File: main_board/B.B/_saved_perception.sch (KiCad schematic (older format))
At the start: 10 parts

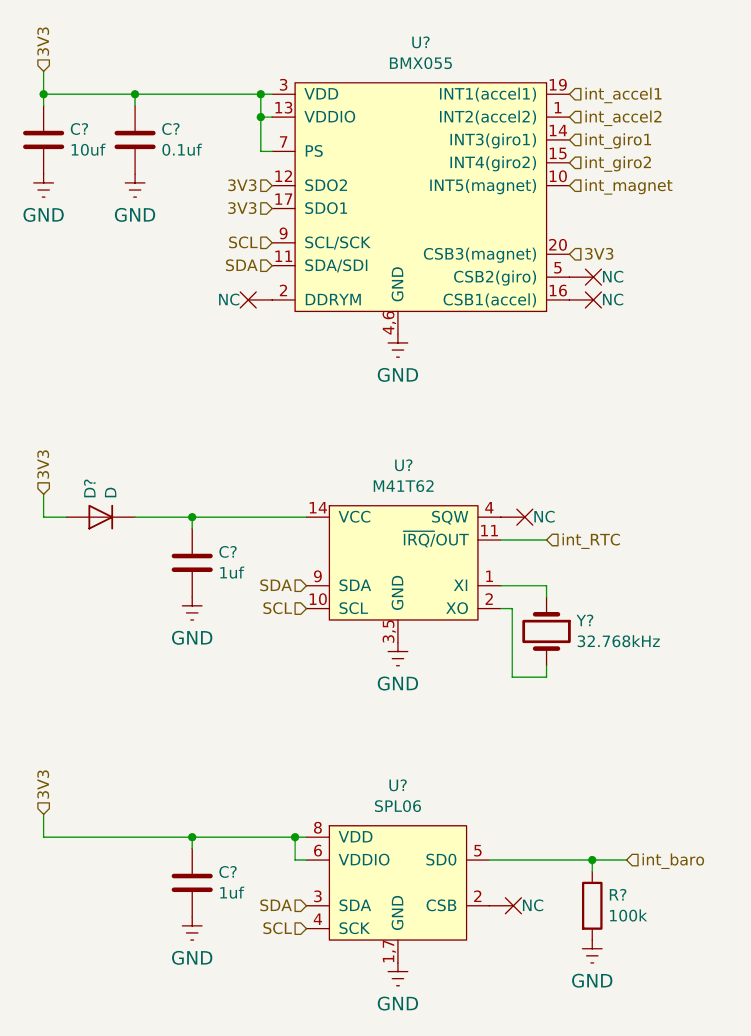
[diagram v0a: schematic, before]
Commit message: interrupt
all interapt on PCA9555
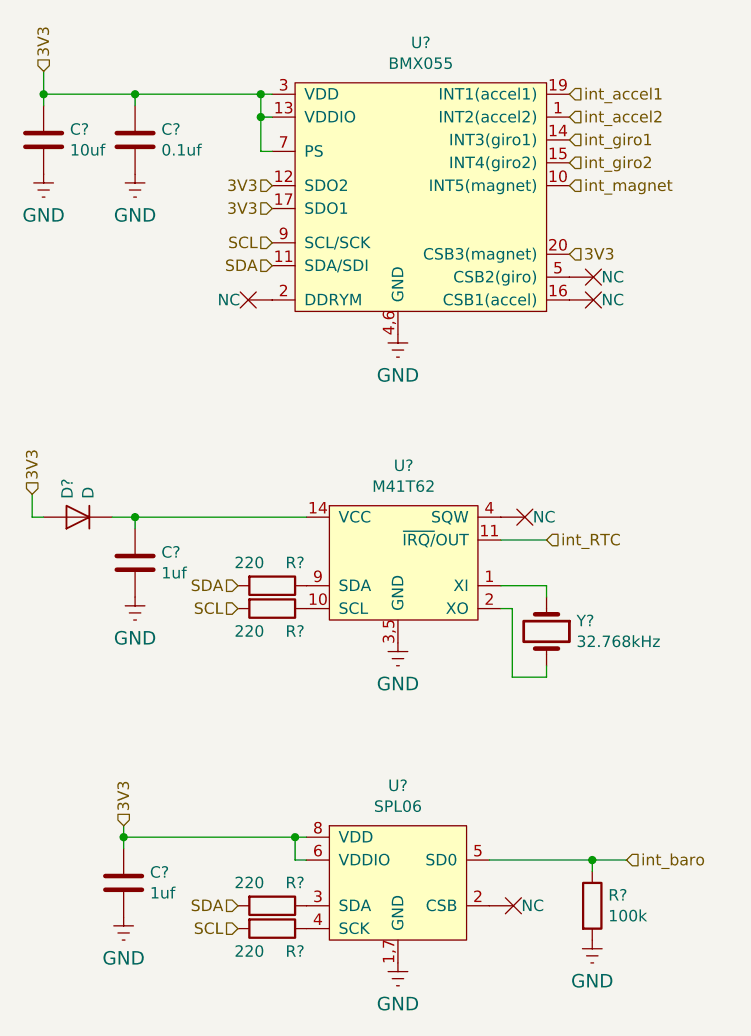
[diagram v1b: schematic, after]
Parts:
- added R? (x4): 220, symbol Device:R
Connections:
- net SCL: now also R?.2, R?.2; no longer U?.10 (SCL), U?.4 (SCK)
- net SDA: now also R?.2, R?.2; no longer U?.3 (SDA), U?.9 (SDA)
- new net: R?.1, U?.10 (SCL)
- new net: R?.1, U?.9 (SDA)
- new net: R?.1, U?.3 (SDA)
- new net: R?.1, U?.4 (SCK)
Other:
- moved on the sheet: C?, D?
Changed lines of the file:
@@
 F 1 "M41T62" H 5625 3884 50  0000 C CNN
 F 2 "" H 5600 3750 50  0001 C CNN
-F 3 "" H 5600 3750 50  0001 C CNN
+F 3 "https://datasheet.lcsc.com/szlcsc/STMicroelectronics-M41T62Q6F_C113207.pdf" H 5600 3750 50  0001 C CNN
 	1    5600 3750
 	1    0    0    -1
 $EndComp
-Text HLabel 4050 3650 1    50   Input ~ 0
+Text HLabel 4000 3650 1    50   Input ~ 0
 3V3
 $Comp
 L Device:D D?
 U 1 1 5F93AF19
-P 4300 3750
+P 4200 3750
 AR Path="/5F96CFDA/5F93AF19" Ref="D?"  Part="1"
 AR Path="/5F9EE529/5F9F24D4/5F93AF19" Ref="D?"  Part="1"
 AR Path="/5FA9DBB3/5F9F24D4/5F93AF19" Ref="D?"  Part="1"
-F 0 "D?" V 4346 3670 50  0000 R CNN
-F 1 "D" V 4255 3670 50  0000 R CNN
-F 2 "BB:SOD-323" H 4300 3750 50  0001 C CNN
-F 3 "https://datasheet.lcsc.com/szlcsc/SK-SD103AWS_C109204.pdf" H 4300 3750 50  0001 C CNN
-F 4 "C109204" V 4300 3750 50  0001 C CNN "LCSC"
-	1    4300 3750
+F 0 "D?" V 4246 3670 50  0000 R CNN
+F 1 "D" V 4155 3670 50  0000 R CNN
+F 2 "BB:SOD-323" H 4200 3750 50  0001 C CNN
+F 3 "https://datasheet.lcsc.com/szlcsc/SK-SD103AWS_C109204.pdf" H 4200 3750 50  0001 C CNN
+F 4 "C109204" V 4200 3750 50  0001 C CNN "LCSC"
+	1    4200 3750
 	-1   0    0    1
 $EndComp
 Wire Wire Line
-	4150 3750 4050 3750
-Wire Wire Line
-	4050 3750 4050 3650
+	4050 3750 4000 3750
+Wire Wire Line
+	4000 3750 4000 3650
 $Comp
 L Device:Crystal Y?
@@
 Wire Wire Line
 	6250 4450 6250 4400
-Text HLabel 5200 4050 0    50   Input ~ 0
-SDA
-Text HLabel 5200 4150 0    50   Input ~ 0
-SCL
 $Comp
 L B.B-eagle-import:GND #GND?
@@
 L B.B-eagle-import:GND #GND?
 U 1 1 5F94A059
-P 4700 4200
+P 4450 4200
 AR Path="/5F96CFDA/5F94A059" Ref="#GND?"  Part="1"
 AR Path="/5F9EE529/5F9F24D4/5F94A059" Ref="#GND?"  Part="1"
 AR Path="/5FA9DBB3/5F9F24D4/5F94A059" Ref="#GND?"  Part="1"
-F 0 "#GND?" H 4700 4200 50  0001 C CNN
-F 1 "GND" H 4700 4120 59  0000 C CNN
-F 2 "" H 4700 4200 50  0001 C CNN
-F 3 "" H 4700 4200 50  0001 C CNN
-	1    4700 4200
-	1    0    0    -1
-$EndComp
-Wire Wire Line
-	4700 3800 4700 3750
+F 0 "#GND?" H 4450 4200 50  0001 C CNN
+F 1 "GND" H 4450 4120 59  0000 C CNN
+F 2 "" H 4450 4200 50  0001 C CNN
+F 3 "" H 4450 4200 50  0001 C CNN
+	1    4450 4200
+	1    0    0    -1
+$EndComp
+Wire Wire Line
+	4450 3800 4450 3750
 $Comp
 L B.B-eagle-import:NC #NC?
@@
 	1    0    0    -1
 $EndComp
-Text HLabel 5200 5550 0    50   Input ~ 0
+Text HLabel 4900 5550 0    50   Input ~ 0
 SCL
-Text HLabel 5200 5450 0    50   Input ~ 0
+Text HLabel 4900 5450 0    50   Input ~ 0
 SDA
 Connection ~ 6450 5250
@@
 	-1   0    0    1
 $EndComp
-Text HLabel 4050 5050 1    50   Input ~ 0
+Text HLabel 4400 5100 1    50   Input ~ 0
 3V3
-Wire Wire Line
-	4050 5050 4050 5150
-Wire Wire Line
-	4050 5150 4700 5150
 $Comp
 L Device:C C?
 U 1 1 5F975C33
-P 4700 5350
+P 4400 5350
 AR Path="/5F96CFDA/5F975C33" Ref="C?"  Part="1"
 AR Path="/5F9EE529/5F9F24D4/5F975C33" Ref="C?"  Part="1"
 AR Path="/5FA9DBB3/5F9F24D4/5F975C33" Ref="C?"  Part="1"
-F 0 "C?" H 4815 5396 50  0000 L CNN
-F 1 "1uf" H 4815 5305 50  0000 L CNN
-F 2 "Resistor_SMD:R_0402_1005Metric" H 4738 5200 50  0001 C CNN
-F 3 "~" H 4700 5350 50  0001 C CNN
-F 4 "C52923" H 4700 5350 50  0001 C CNN "LCSC"
-	1    4700 5350
+F 0 "C?" H 4515 5396 50  0000 L CNN
+F 1 "1uf" H 4515 5305 50  0000 L CNN
+F 2 "Resistor_SMD:R_0402_1005Metric" H 4438 5200 50  0001 C CNN
+F 3 "~" H 4400 5350 50  0001 C CNN
+F 4 "C52923" H 4400 5350 50  0001 C CNN "LCSC"
+	1    4400 5350
 	1    0    0    -1
 $EndComp
@@
 L B.B-eagle-import:GND #GND?
 U 1 1 5F975C39
-P 4700 5600
+P 4400 5600
 AR Path="/5F96CFDA/5F975C39" Ref="#GND?"  Part="1"
 AR Path="/5F9EE529/5F9F24D4/5F975C39" Ref="#GND?"  Part="1"
 AR Path="/5FA9DBB3/5F9F24D4/5F975C39" Ref="#GND?"  Part="1"
-F 0 "#GND?" H 4700 5600 50  0001 C CNN
-F 1 "GND" H 4700 5520 59  0000 C CNN
-F 2 "" H 4700 5600 50  0001 C CNN
-F 3 "" H 4700 5600 50  0001 C CNN
-	1    4700 5600
-	1    0    0    -1
-$EndComp
-Wire Wire Line
-	4700 5200 4700 5150
+F 0 "#GND?" H 4400 5600 50  0001 C CNN
+F 1 "GND" H 4400 5520 59  0000 C CNN
+F 2 "" H 4400 5600 50  0001 C CNN
+F 3 "" H 4400 5600 50  0001 C CNN
+	1    4400 5600
+	1    0    0    -1
+$EndComp
+Wire Wire Line
+	4400 5200 4400 5150
 $Comp
 L Device:C C?
 U 1 1 5F9780C8
-P 4700 3950
+P 4450 3950
 AR Path="/5F96CFDA/5F9780C8" Ref="C?"  Part="1"
 AR Path="/5F9EE529/5F9F24D4/5F9780C8" Ref="C?"  Part="1"
 AR Path="/5FA9DBB3/5F9F24D4/5F9780C8" Ref="C?"  Part="1"
-F 0 "C?" H 4815 3996 50  0000 L CNN
-F 1 "1uf" H 4815 3905 50  0000 L CNN
-F 2 "Resistor_SMD:R_0402_1005Metric" H 4738 3800 50  0001 C CNN
-F 3 "~" H 4700 3950 50  0001 C CNN
-F 4 "C52923" H 4700 3950 50  0001 C CNN "LCSC"
-	1    4700 3950
-	1    0    0    -1
-$EndComp
-Connection ~ 4700 5150
-Wire Wire Line
-	4700 5150 5150 5150
-Connection ~ 4700 3750
-Wire Wire Line
-	4700 3750 5200 3750
-Wire Wire Line
-	4450 3750 4700 3750
+F 0 "C?" H 4565 3996 50  0000 L CNN
+F 1 "1uf" H 4565 3905 50  0000 L CNN
+F 2 "Resistor_SMD:R_0402_1005Metric" H 4488 3800 50  0001 C CNN
+F 3 "~" H 4450 3950 50  0001 C CNN
+F 4 "C52923" H 4450 3950 50  0001 C CNN "LCSC"
+	1    4450 3950
+	1    0    0    -1
+$EndComp
+Connection ~ 4400 5150
+Wire Wire Line
+	4400 5150 5150 5150
+Connection ~ 4450 3750
+Wire Wire Line
+	4450 3750 5200 3750
+Wire Wire Line
+	4350 3750 4450 3750
 Wire Wire Line
 	5200 5250 5150 5250
 Wire Wire Line
 	5150 5250 5150 5150
-Connection ~ 5150 5150
 Wire Wire Line
 	5150 5150 5200 5150
@@
 	1    0    0    -1
 $EndComp
+$Comp
+L Device:R R?
+U 1 1 5FAFDE55
+P 5050 5450
+AR Path="/5FA3274C/5FAFDE55" Ref="R?"  Part="1"
+AR Path="/5F9EE529/5FAFDE55" Ref="R?"  Part="1"
+AR Path="/5F9EE529/5F9F24D4/5FAFDE55" Ref="R?"  Part="1"
+F 0 "R?" V 4950 5550 50  0000 C CNN
+F 1 "220" V 4950 5350 50  0000 C CNN
+F 2 "" V 4980 5450 50  0001 C CNN
+F 3 "~" H 5050 5450 50  0001 C CNN
+F 4 "C25092" V 5050 5450 50  0001 C CNN "LCSC"
+	1    5050 5450
+	0    1    1    0
+$EndComp
+$Comp
+L Device:R R?
+U 1 1 5FAFE429
+P 5050 5550
+AR Path="/5FA3274C/5FAFE429" Ref="R?"  Part="1"
+AR Path="/5F9EE529/5FAFE429" Ref="R?"  Part="1"
+AR Path="/5F9EE529/5F9F24D4/5FAFE429" Ref="R?"  Part="1"
+F 0 "R?" V 5150 5650 50  0000 C CNN
+F 1 "220" V 5150 5450 50  0000 C CNN
+F 2 "" V 4980 5550 50  0001 C CNN
+F 3 "~" H 5050 5550 50  0001 C CNN
+F 4 "C25092" V 5050 5550 50  0001 C CNN "LCSC"
+	1    5050 5550
+	0    1    1    0
+$EndComp
+Connection ~ 5150 5150
+Text HLabel 4900 4150 0    50   Input ~ 0
+SCL
+Text HLabel 4900 4050 0    50   Input ~ 0
+SDA
+$Comp
+L Device:R R?
+U 1 1 5FB01470
+P 5050 4050
+AR Path="/5FA3274C/5FB01470" Ref="R?"  Part="1"
+AR Path="/5F9EE529/5FB01470" Ref="R?"  Part="1"
+AR Path="/5F9EE529/5F9F24D4/5FB01470" Ref="R?"  Part="1"
+F 0 "R?" V 4950 4150 50  0000 C CNN
+F 1 "220" V 4950 3950 50  0000 C CNN
+F 2 "" V 4980 4050 50  0001 C CNN
+F 3 "~" H 5050 4050 50  0001 C CNN
+F 4 "C25092" V 5050 4050 50  0001 C CNN "LCSC"
+	1    5050 4050
+	0    1    1    0
+$EndComp
+$Comp
+L Device:R R?
+U 1 1 5FB01477
+P 5050 4150
+AR Path="/5FA3274C/5FB01477" Ref="R?"  Part="1"
+AR Path="/5F9EE529/5FB01477" Ref="R?"  Part="1"
+AR Path="/5F9EE529/5F9F24D4/5FB01477" Ref="R?"  Part="1"
+F 0 "R?" V 5150 4250 50  0000 C CNN
+F 1 "220" V 5150 4050 50  0000 C CNN
+F 2 "" V 4980 4150 50  0001 C CNN
+F 3 "~" H 5050 4150 50  0001 C CNN
+F 4 "C25092" V 5050 4150 50  0001 C CNN "LCSC"
+	1    5050 4150
+	0    1    1    0
+$EndComp
+Wire Wire Line
+	4400 5100 4400 5150
 $EndSCHEMATC
